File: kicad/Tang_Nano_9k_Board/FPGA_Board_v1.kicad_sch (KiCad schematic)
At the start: 28 parts, among them J1 Conn_01x24, J2 Conn_01x24, J3 Conn_01x08, J4 Conn_01x04, J5 Conn_01x04, J6 Conn_01x04, J7 Conn_01x04, SW1 SW_DIP_x08, SW2 SW_Push, SW3 SW_Push, SW4 SW_Push, U3 TBD62083AFG, U4 74HC138, U6 TBD62786APG

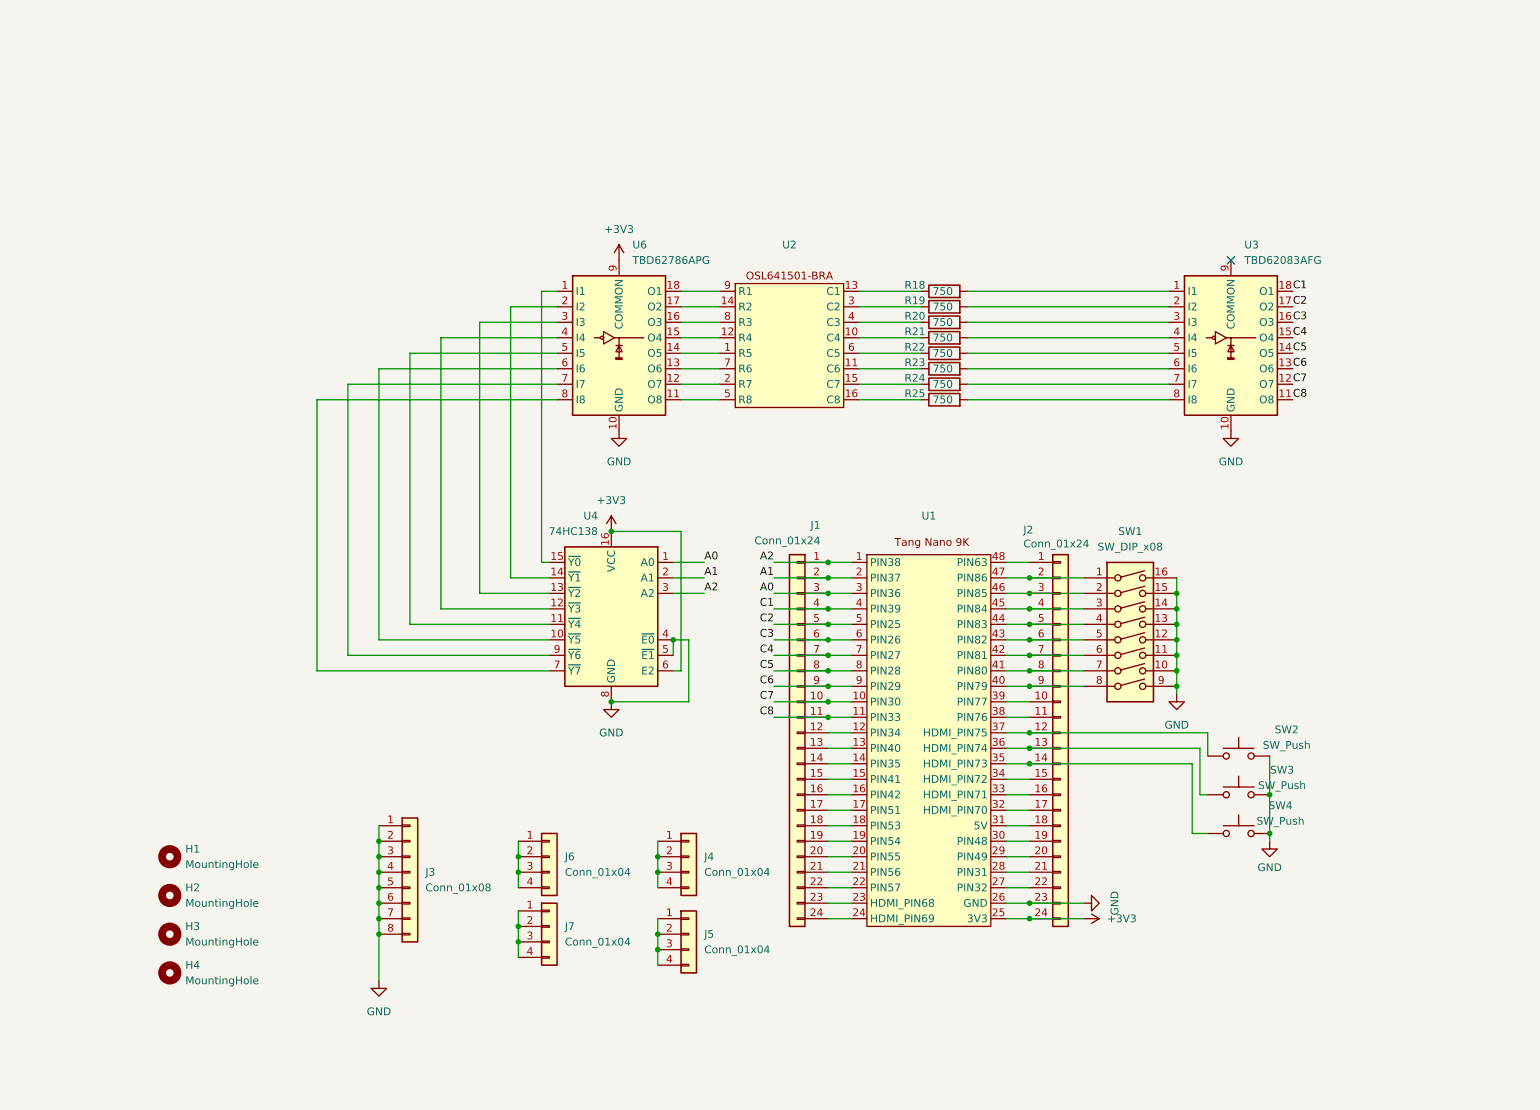
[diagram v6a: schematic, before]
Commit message: finish schematic, design PCB board
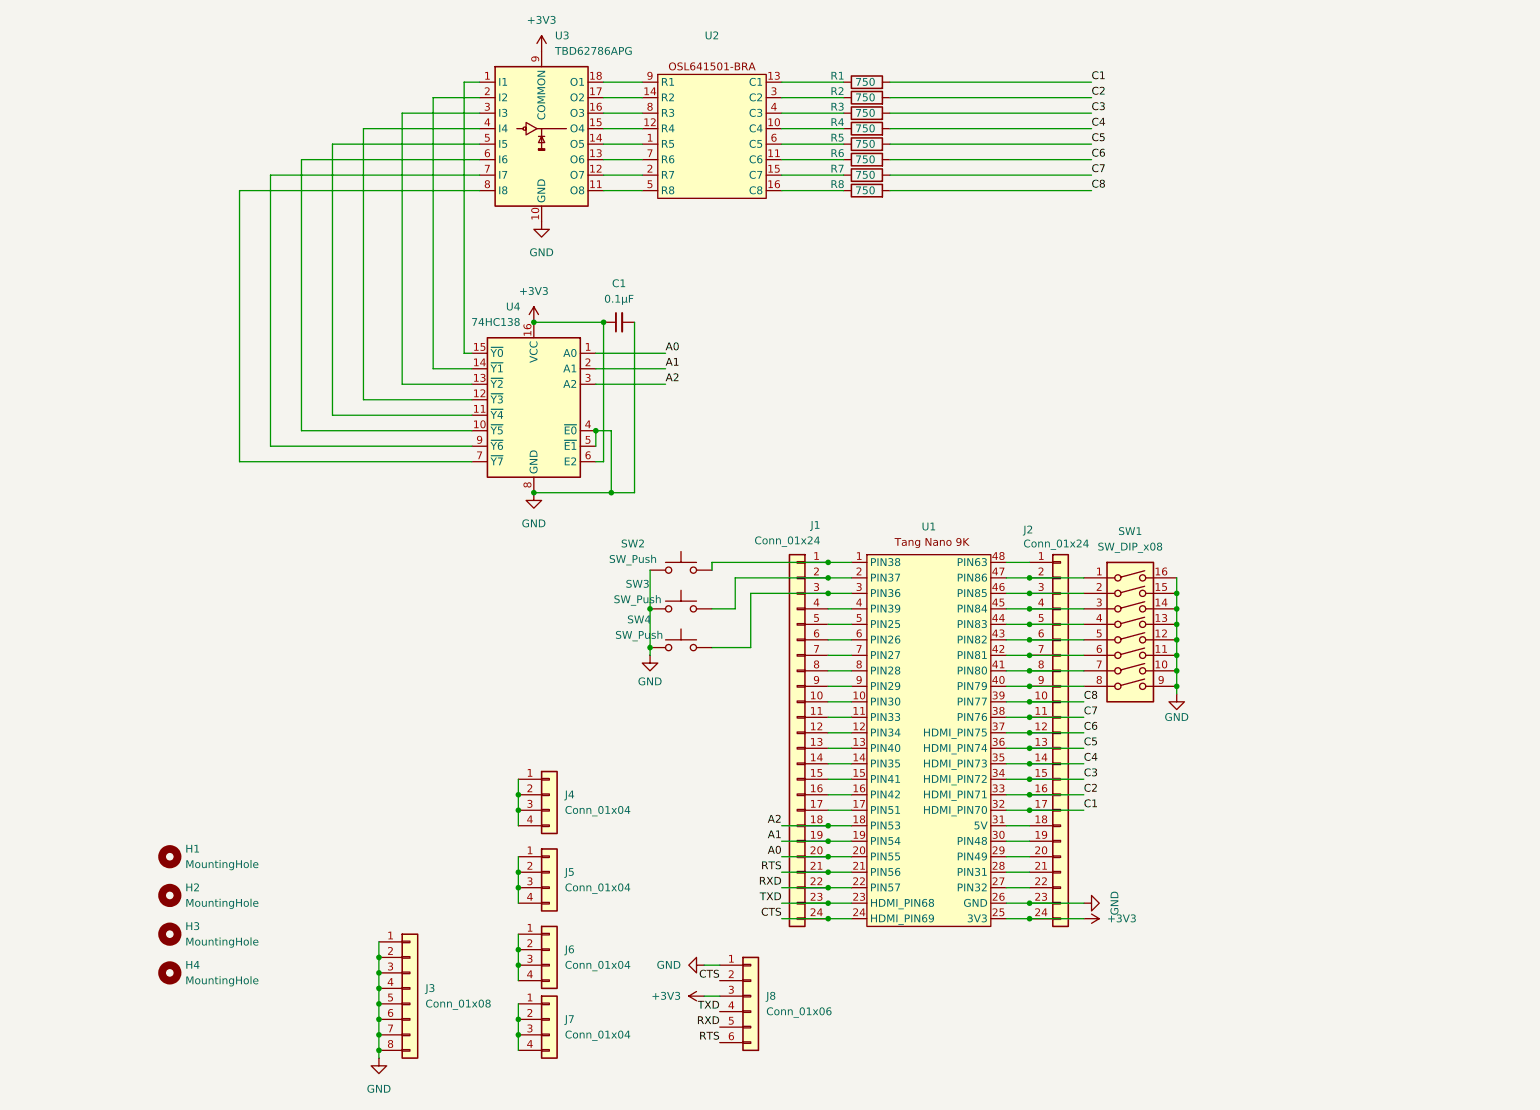
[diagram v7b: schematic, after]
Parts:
- removed U3: TBD62083AFG, Package_DIP:DIP-18_W7.62mm, symbol yuma_bf:TBD62083AFG
- added C1: 0.1μF, Capacitor_SMD:C_0603_1608Metric, symbol Device:C_Small
- added J8: Conn_01x06, Connector_PinHeader_2.54mm:PinHeader_1x06_P2.54mm_Vertical, symbol Connector_Generic:Conn_01x06
- renumbered R18 to R1, R19 to R2, R20 to R3, R21 to R4, R22 to R5, R23 to R6, R24 to R7, R25 to R8, U6 to U3
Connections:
- net +3V3: now also C1.1, J8.3 (Pin_3)
- net A0: now also J1.20 (Pin_20), U1.20 (PIN55); no longer J1.3 (Pin_3), U1.3 (PIN36)
- net A1: now also J1.19 (Pin_19), U1.19 (PIN54); no longer J1.2 (Pin_2), U1.2 (PIN37)
- net A2: now also J1.18 (Pin_18), U1.18 (PIN53); no longer J1.1 (Pin_1), U1.1 (PIN38)
- net C1: now also J2.17 (Pin_17), R1.2, U1.32 (HDMI_PIN70); no longer J1.4 (Pin_4), U1.4 (PIN39)
- net C2: now also J2.16 (Pin_16), R2.2, U1.33 (HDMI_PIN71); no longer J1.5 (Pin_5), U1.5 (PIN25)
- net C3: now also J2.15 (Pin_15), R3.2, U1.34 (HDMI_PIN72); no longer J1.6 (Pin_6), U1.6 (PIN26)
- net C4: now also J2.14 (Pin_14), R4.2, U1.35 (HDMI_PIN73); no longer J1.7 (Pin_7), U1.7 (PIN27)
- net C5: now also J2.13 (Pin_13), R5.2, U1.36 (HDMI_PIN74); no longer J1.8 (Pin_8), U1.8 (PIN28)
- net C6: now also J2.12 (Pin_12), R6.2, U1.37 (HDMI_PIN75); no longer J1.9 (Pin_9), U1.9 (PIN29)
- net C7: now also J2.11 (Pin_11), R7.2, U1.38 (PIN76); no longer J1.10 (Pin_10), U1.10 (PIN30)
- net C8: now also J2.10 (Pin_10), R8.2, U1.39 (PIN77); no longer J1.11 (Pin_11), U1.11 (PIN33)
- net GND: now also C1.2, J8.1 (Pin_1)
- net RTS: now reaches J1.21 (Pin_21), U1.21 (PIN56)
- net RTS: now also J8.6 (Pin_6)
- net RXD: now reaches J1.22 (Pin_22), U1.22 (PIN57)
- net RXD: now also J8.5 (Pin_5)
- net TXD: now reaches J1.23 (Pin_23), U1.23 (HDMI_PIN68)
- net TXD: now also J8.4 (Pin_4)
- net CTS: now reaches J1.24 (Pin_24), U1.24 (HDMI_PIN69)
- net CTS: now also J8.2 (Pin_2)
- new net: J1.1 (Pin_1), SW2.1, U1.1 (PIN38)
- new net: J1.10 (Pin_10), U1.10 (PIN30)
- new net: J1.11 (Pin_11), U1.11 (PIN33)
- new net: J1.2 (Pin_2), SW3.1, U1.2 (PIN37)
- new net: J1.3 (Pin_3), SW4.1, U1.3 (PIN36)
- new net: J1.4 (Pin_4), U1.4 (PIN39)
- new net: J1.5 (Pin_5), U1.5 (PIN25)
- new net: J1.6 (Pin_6), U1.6 (PIN26)
- new net: J1.7 (Pin_7), U1.7 (PIN27)
- new net: J1.8 (Pin_8), U1.8 (PIN28)
- new net: J1.9 (Pin_9), U1.9 (PIN29)
- no-connect marks 1 -> 0
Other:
- moved on the sheet: J3, J4, J5, J6, J7, R1, R2, R3, R4, R5, R6, R7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

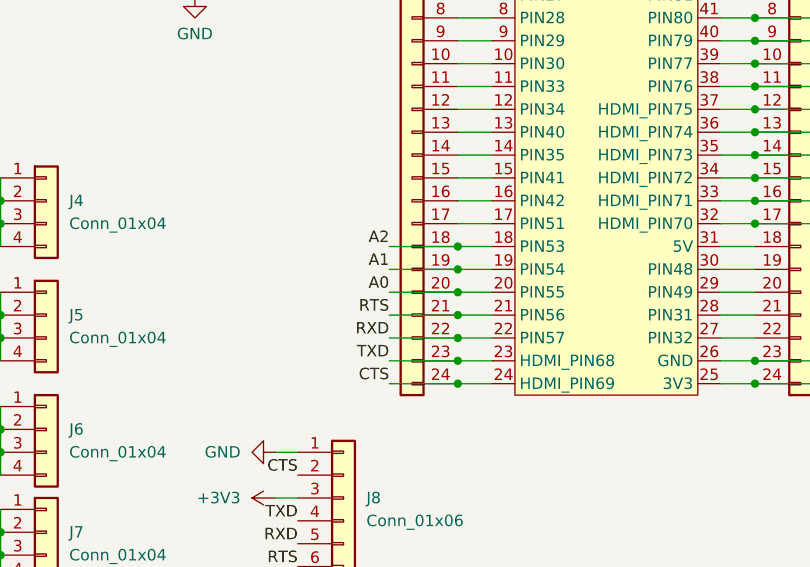
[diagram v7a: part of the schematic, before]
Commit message: modify shematic, shift the UART pin up
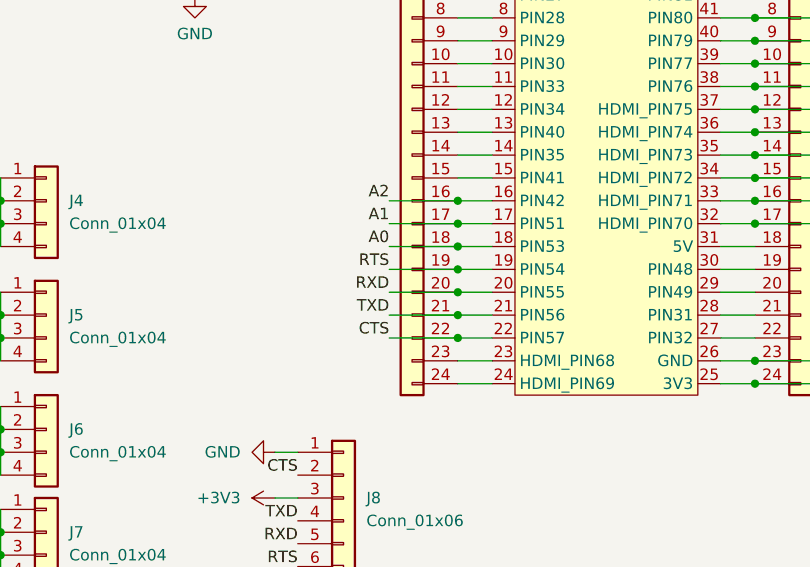
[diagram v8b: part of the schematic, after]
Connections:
- net A0: now also J1.18 (Pin_18), U1.18 (PIN53); no longer J1.20 (Pin_20), U1.20 (PIN55)
- net A1: now also J1.17 (Pin_17), U1.17 (PIN51); no longer J1.19 (Pin_19), U1.19 (PIN54)
- net A2: now also J1.16 (Pin_16), U1.16 (PIN42); no longer J1.18 (Pin_18), U1.18 (PIN53)
- net CTS: now also J1.22 (Pin_22), U1.22 (PIN57); no longer J1.24 (Pin_24), U1.24 (HDMI_PIN69)
- net RTS: now also J1.19 (Pin_19), U1.19 (PIN54); no longer J1.21 (Pin_21), U1.21 (PIN56)
- net RXD: now also J1.20 (Pin_20), U1.20 (PIN55); no longer J1.22 (Pin_22), U1.22 (PIN57)
- net TXD: now also J1.21 (Pin_21), U1.21 (PIN56); no longer J1.23 (Pin_23), U1.23 (HDMI_PIN68)
- new net: J1.23 (Pin_23), U1.23 (HDMI_PIN68)
- new net: J1.24 (Pin_24), U1.24 (HDMI_PIN69)
